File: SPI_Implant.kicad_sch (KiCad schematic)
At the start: 10 parts, among them J1 Dediprog_FPC, J2 SPI_Socket, U1 W25Q32JVSS, U2 W25Q32JVSS, U3 TMUX1511PWR, U4 TMUX1511PWR

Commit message: Fixed ERC errors
Signed-off-by: Andy Ebrahiem <andy@9elements.com>
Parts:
- removed J1: Dediprog_FPC, Connector_FFC-FPC:TE_84952-9_1x09-1MP_P1.0mm_Horizontal, symbol Connector:Conn_01x09_Socket
- removed U1, U2: W25Q32JVSS, Package_SO:SOIC-8_5.23x5.23mm_P1.27mm, symbol Memory_Flash:W25Q32JVSS
- added J1: Conn_01x10_Socket, symbol Connector:Conn_01x10_Socket
- added R3, R4, R5: 100, Resistor_SMD:R_0603_1608Metric, symbol Device:R
- R1, R2: value 10K -> 100; footprint (none) -> Resistor_SMD:R_0603_1608Metric
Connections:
- net +3.3V: now also J1.2 (Pin_2); no longer R1.1, R2.1
- net CLK: now also R1.2; no longer J2.4 (Pin_4)
- net CS1: no longer R1.2
- net CS2: no longer R2.2
- net GND: now also J1.1 (Pin_1)
- net IO2: now also R4.2; no longer J2.7 (Pin_7)
- net IO3: now also R5.2; no longer J2.8 (Pin_8)
- net MISO: now also R2.2; no longer J2.5 (Pin_5)
- net MOSI: now also R3.2; no longer J2.6 (Pin_6)
- net P_CLK: now also J1.4 (Pin_4)
- net P_CS1: now also J1.3 (Pin_3)
- net P_CS2: now also J1.9 (Pin_9)
- net P_IO2: now also J1.7 (Pin_7)
- net P_IO3: now also J1.8 (Pin_8)
- net P_MISO: now also J1.5 (Pin_5)
- net P_MOSI: now also J1.6 (Pin_6)
- new net: J2.7 (Pin_7), R4.1
- new net: J2.8 (Pin_8), R5.1
- new net: J2.4 (Pin_4), R1.1
- new net: J2.6 (Pin_6), R3.1
- new net: J2.5 (Pin_5), R2.1
- no-connect marks 1 -> 2

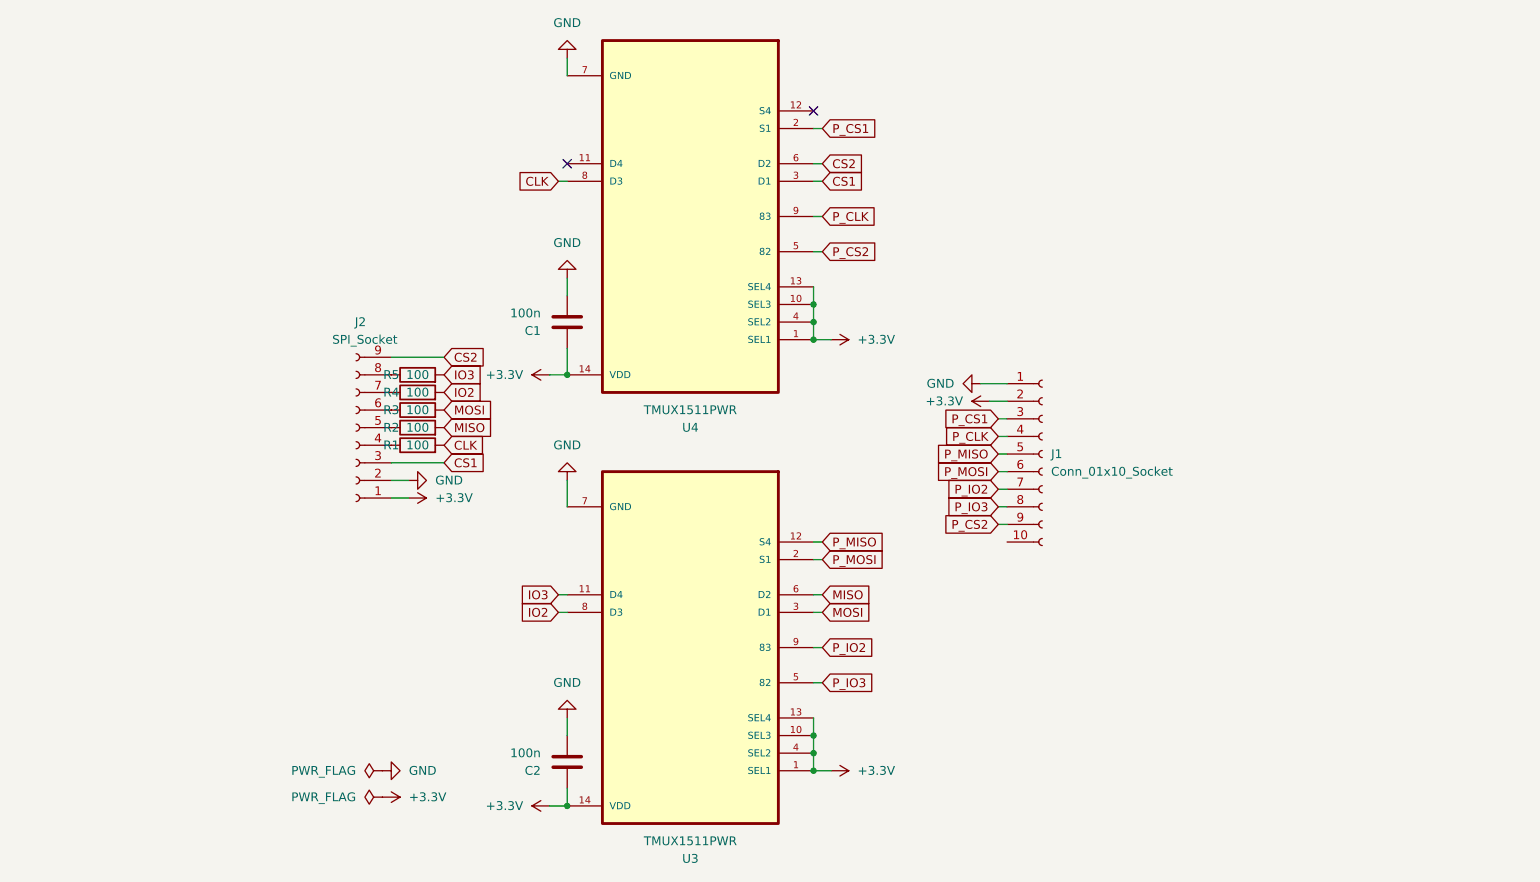
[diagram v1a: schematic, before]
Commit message: updated footprints and routing, added labels
Signed-off-by: Andy Ebrahiem <andy@9elements.com>
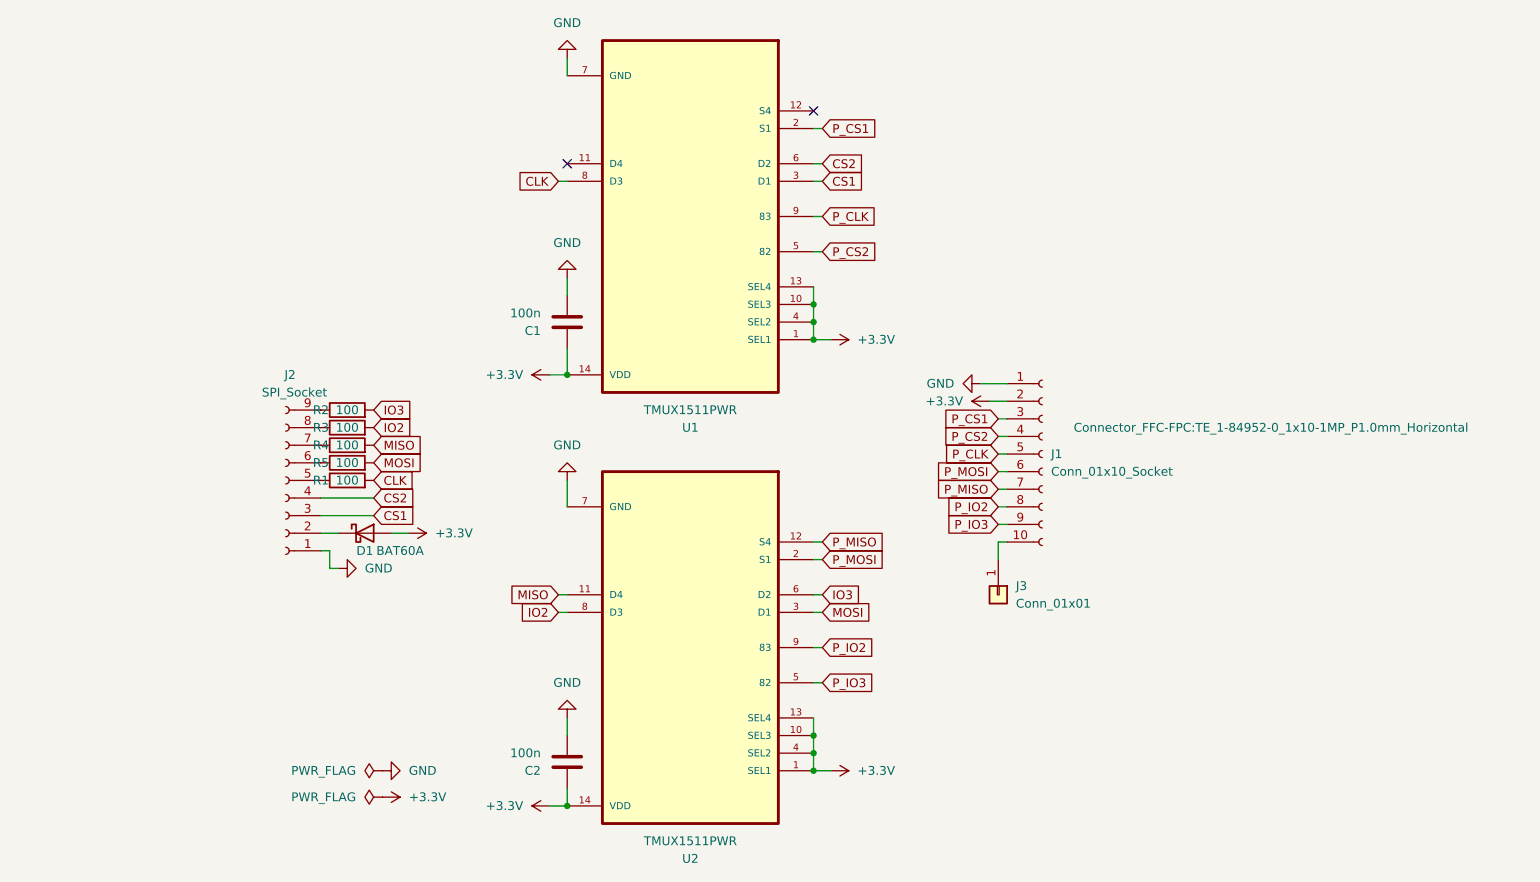
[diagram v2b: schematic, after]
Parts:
- added D1: BAT60A, Diode_SMD:D_SOD-323, symbol Diode:BAT60A
- added J3: Conn_01x01, Connector_Wire:SolderWirePad_1x01_SMD_1x2mm, symbol Connector_Generic:Conn_01x01
- C1, C2: footprint Capacitor_SMD:C_0603_1608Metric -> Capacitor_SMD:C_0805_2012Metric
- J1: footprint (none) -> Connector_FFC-FPC:TE_1-84952-0_1x10-1MP_P1.0mm_Horizontal
- J2: footprint Connector_PinSocket_1.27mm:PinSocket_1x10_P1.27mm_Vertical -> pad:wire_pad_row_1x09-2x3mm
- R1, R2, R3, R4, R5: footprint Resistor_SMD:R_0603_1608Metric -> Resistor_SMD:R_0805_2012Metric
- renumbered U4 to U1, U3 to U2
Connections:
- net +3.3V: now also D1.2 (A); no longer J2.1 (Pin_1)
- net CS2: now also J2.4 (Pin_4); no longer J2.9 (Pin_9)
- net GND: now also J2.1 (Pin_1); no longer J2.2 (Pin_2)
- net IO2: now also R3.2; no longer R4.2
- net IO3: now also R2.2, U2.6 (D2); no longer R5.2, U2.11 (D4)
- net MISO: now also R4.2, U2.11 (D4); no longer R2.2, U2.6 (D2)
- net MOSI: now also R5.2; no longer R3.2
- net P_CLK: now also J1.5 (Pin_5); no longer J1.4 (Pin_4)
- net P_CS2: now also J1.4 (Pin_4); no longer J1.9 (Pin_9)
- net P_IO2: now also J1.8 (Pin_8); no longer J1.7 (Pin_7)
- net P_IO3: now also J1.9 (Pin_9); no longer J1.8 (Pin_8)
- net P_MISO: now also J1.7 (Pin_7); no longer J1.5 (Pin_5)
- net at J2.8 (Pin_8): now also R3.1; no longer R5.1
- net at R1.1: now also J2.5 (Pin_5); no longer J2.4 (Pin_4)
- net at J2.6 (Pin_6): now also R5.1; no longer R3.1
- net at R2.1: now also J2.9 (Pin_9); no longer J2.5 (Pin_5)
- net at J1.10 (Pin_10): now also J3.1 (Pin_1)
- new net: D1.1 (K), J2.2 (Pin_2)
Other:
- moved on the sheet: J2
